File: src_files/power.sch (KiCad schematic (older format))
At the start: 44 parts, among them J6 Conn_01x02, U1 MCP1700-1202E_SOT23, U2 AX1007E18A, U3 ME6211A33PG-N, U5 MCP1700-3302E_SOT23, U6 TPS54332DDA

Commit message: updated all files and production files as well
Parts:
- FB3: footprint Resistor_SMD:R_0603_1608Metric -> Inductor_SMD:L_0603_1608Metric
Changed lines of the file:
@@
 F 0 "FB3" V 10003 1125 39  0000 C CNN
 F 1 "FBMJ1608HS280NTR" V 10054 1125 39  0001 C CNN
-F 2 "Resistor_SMD:R_0603_1608Metric" V 10130 1125 50  0001 C CNN
+F 2 "Inductor_SMD:L_0603_1608Metric" V 10130 1125 50  0001 C CNN
 F 3 "~" H 10200 1125 50  0001 C CNN
 F 4 "FBMJ1608HS280NTR" V 10071 1125 30  0000 C CNN "MPN"

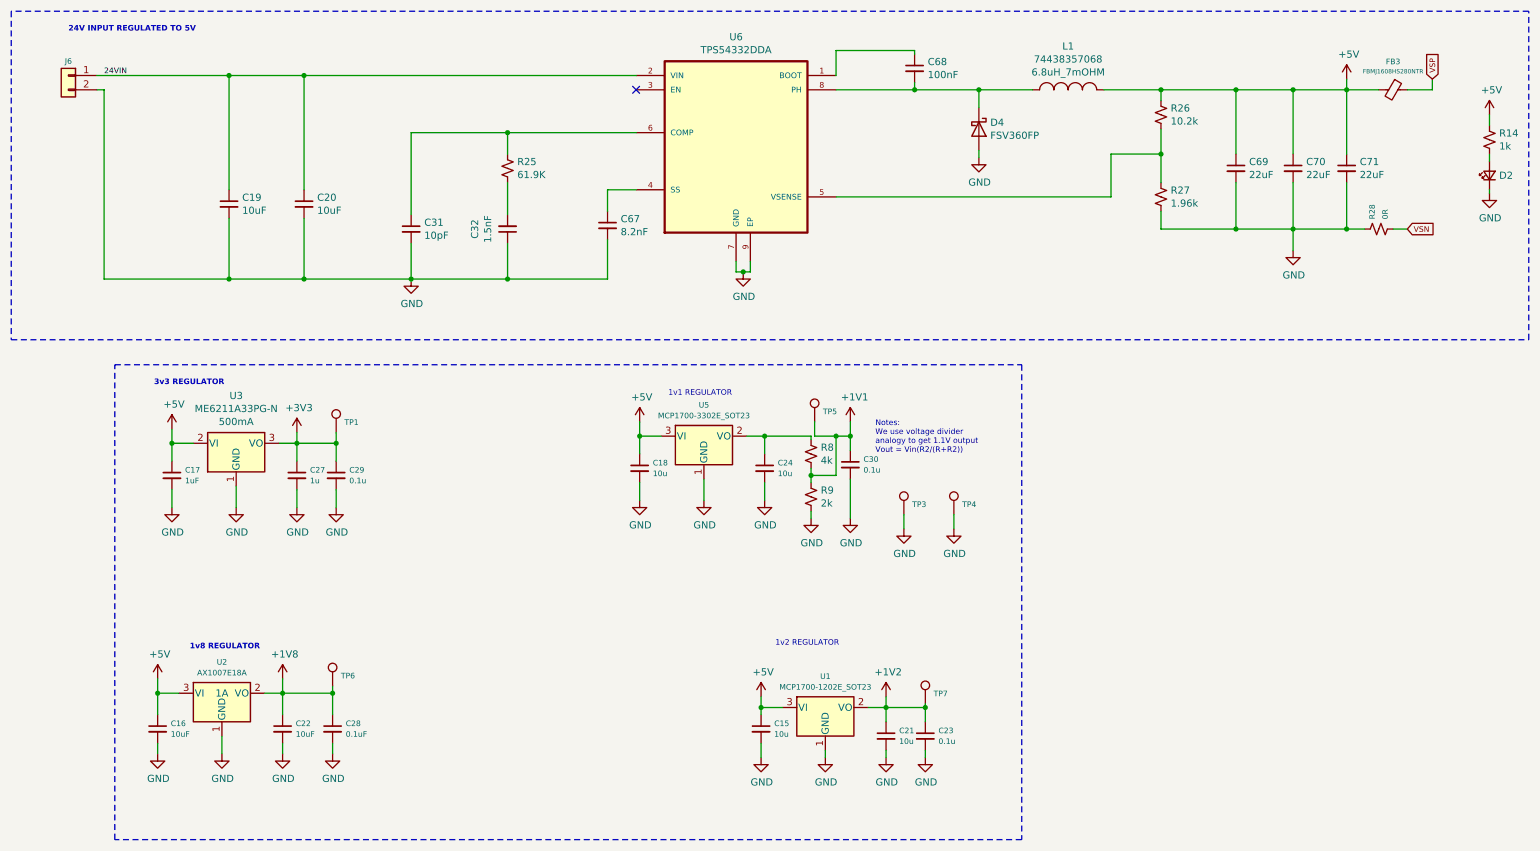
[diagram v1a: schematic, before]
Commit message: update on HDMI to MIPI
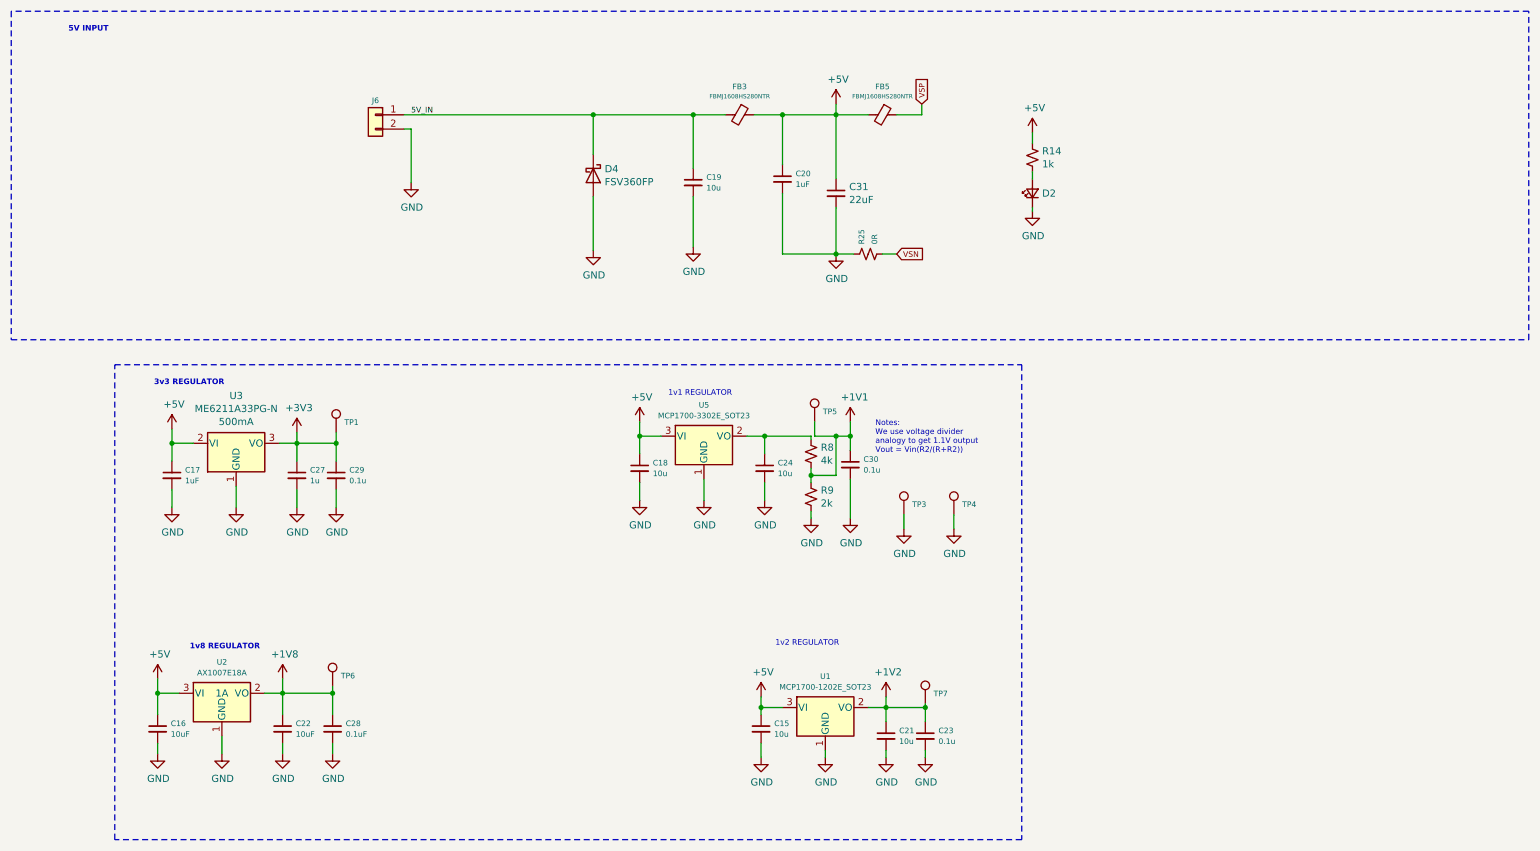
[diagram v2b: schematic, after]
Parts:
- removed C32: 1.5nF, Resistor_SMD:R_0805_2012Metric, symbol Device:C_Small
- removed C67: 8.2nF, Capacitor_SMD:C_1206_3216Metric, symbol Device:C_Small
- removed C68: 100nF, Capacitor_SMD:C_0805_2012Metric, symbol Device:C_Small
- removed C69, C70, C71: 22uF, Resistor_SMD:R_0201_0603Metric, symbol Device:C_Small
- removed L1: 74438357068, 74438357068_ind:74438357068, symbol OLIMEX_RCL:INDUCTOR_SMALL
- removed R26: 10.2k, Resistor_SMD:R_0603_1608Metric, symbol Device:R_Small_US
- removed R27: 1.96k, Resistor_SMD:R_0603_1608Metric, symbol Device:R_Small_US
- removed R28: 0R, Resistor_SMD:R_0603_1608Metric, symbol Device:R_Small_US
- removed U6: TPS54332DDA, TPS54332:NOPB, symbol TPS54332DDA:TPS54332DDA
- added FB5: FBMJ1608HS280NTR, Inductor_SMD:L_0603_1608Metric, symbol Device:Ferrite_Bead_Small
- C19: value 10uF -> 10u; footprint Resistor_SMD:R_0805_2012Metric -> Capacitor_SMD:C_0603_1608Metric; MPN GRM21BR61E106KA73L -> (none); Supplier DigiKey -> (none)
- C20: value 10uF -> 1uF; footprint Resistor_SMD:R_0805_2012Metric -> Capacitor_SMD:C_0603_1608Metric; MPN GRM21BR61E106KA73L -> (none); Supplier DigiKey -> (none)
- C31: value 10pF -> 22uF; footprint Capacitor_SMD:C_0603_1608Metric -> Resistor_SMD:R_0201_0603Metric; MPN GJM1555C1H100JB01D -> GRM188R60J226MEA0D
- R25: value 61.9K -> 0R; MPN RMCF0603FT61K9 -> (none); Supplier DigiKey -> (none)
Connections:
- net +5V: now also C20.1, C31.1, FB3.1, FB5.2; no longer FB3.2
- net GND: now also R25.1
- net VSN: now also R25.2
- net VSP: now also FB5.1; no longer FB3.1
- net 5V_IN: now reaches D4.1 (K)
- net 5V_IN: now also C19.1, FB3.2, J6.1 (Pin_1)
- removed net 24VIN: C19.1, C20.1, J6.1 (Pin_1)
- no-connect marks 1 -> 0
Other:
- note added: "5V INPUT"
- note removed: "24V INPUT REGULATED TO 5V"
- moved on the sheet: D2, D4, J6, R14
